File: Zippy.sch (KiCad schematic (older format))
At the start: 0 parts

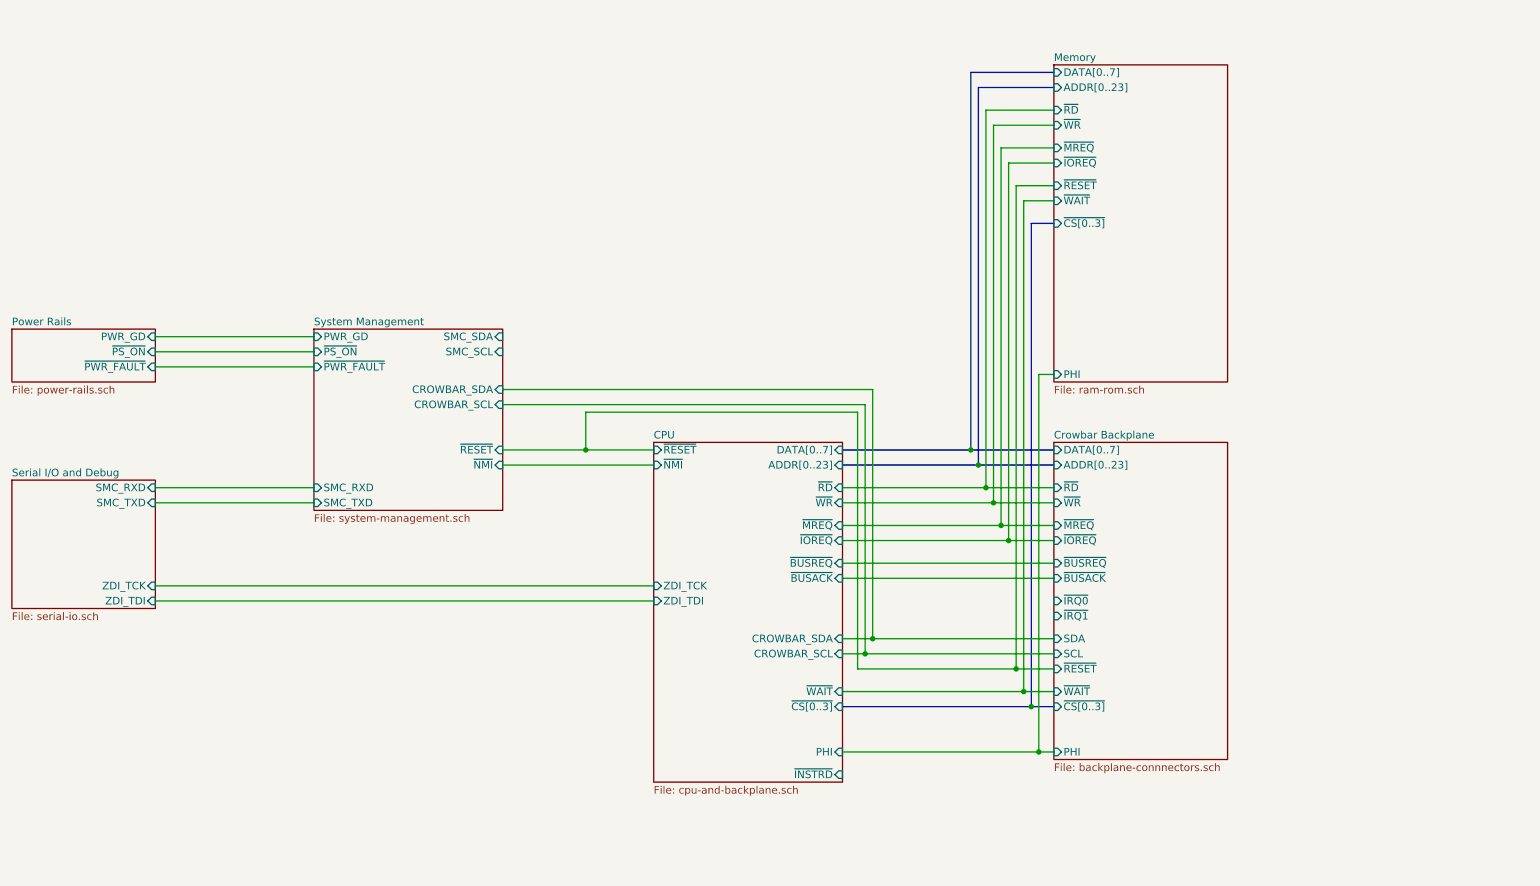
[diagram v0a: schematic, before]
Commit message: crowbar: Reworking the pinout again
  - Completely reworked the pinout of the crowbar bus to match the
    spec.
  - Added lines for eZ80 -> SMC I2C
  - Added lines for SMC -> Crowbar I2C
  - Migrated Crowbar power pinouts to their own sub-sheet
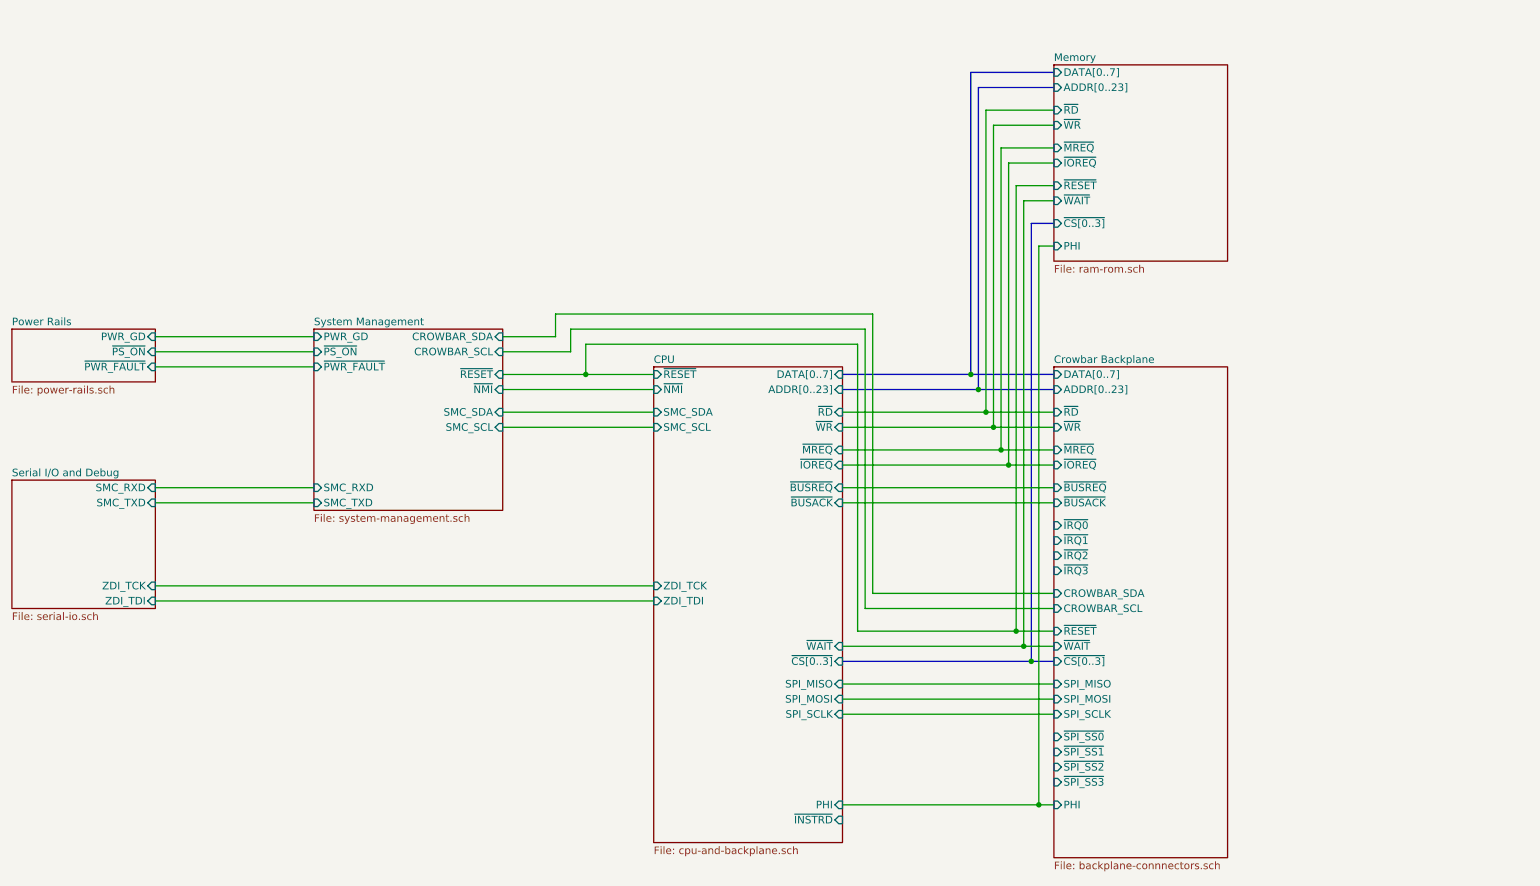
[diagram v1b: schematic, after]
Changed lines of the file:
@@
 $Descr A4 11693 8268
 encoding utf-8
-Sheet 1 7
+Sheet 1 8
 Title ""
 Date ""
@@
 $EndDescr
 $Sheet
-S 5650 3600 1250 2250
+S 5650 3100 1250 3150
 U 5D7F3F15
 F0 "CPU" 50
 F1 "cpu-and-backplane.sch" 50
-F2 "~RESET" I L 5650 3650 50
-F3 "PHI" I R 6900 5650 50
-F4 "ADDR[0..23]" I R 6900 3750 50
-F5 "DATA[0..7]" I R 6900 3650 50
-F6 "~CS[0..3]" I R 6900 5350 50
+F2 "~RESET" I L 5650 3150 50
+F3 "PHI" I R 6900 6000 50
+F4 "ADDR[0..23]" I R 6900 3250 50
+F5 "DATA[0..7]" I R 6900 3150 50
+F6 "~CS[0..3]" I R 6900 5050 50
 F7 "ZDI_TCK" I L 5650 4550 50
 F8 "ZDI_TDI" I L 5650 4650 50
-F9 "~NMI" I L 5650 3750 50
-F10 "CROWBAR_SCL" I R 6900 5000 50
-F11 "CROWBAR_SDA" I R 6900 4900 50
-F12 "~IOREQ" I R 6900 4250 50
-F13 "~MREQ" I R 6900 4150 50
-F14 "~RD" I R 6900 3900 50
-F15 "~WR" I R 6900 4000 50
-F16 "~INSTRD" I R 6900 5800 50
-F17 "~WAIT" I R 6900 5250 50
-F18 "~BUSREQ" I R 6900 4400 50
-F19 "~BUSACK" I R 6900 4500 50
+F9 "~NMI" I L 5650 3250 50
+F10 "~IOREQ" I R 6900 3750 50
+F11 "~MREQ" I R 6900 3650 50
+F12 "~RD" I R 6900 3400 50
+F13 "~WR" I R 6900 3500 50
+F14 "~INSTRD" I R 6900 6100 50
+F15 "~WAIT" I R 6900 4950 50
+F16 "~BUSREQ" I R 6900 3900 50
+F17 "~BUSACK" I R 6900 4000 50
+F18 "SMC_SCL" I L 5650 3500 50
+F19 "SMC_SDA" I L 5650 3400 50
+F20 "SPI_SCLK" I R 6900 5400 50
+F21 "SPI_MISO" I R 6900 5200 50
+F22 "SPI_MOSI" I R 6900 5300 50
 $EndSheet
 $Sheet
@@
 	2350 4650 5650 4650
 Wire Wire Line
-	4650 3650 5200 3650
-Wire Wire Line
-	4650 3750 5650 3750
-$Sheet
-S 8300 3600 1150 2100
+	4650 3150 5200 3150
+Wire Wire Line
+	4650 3250 5650 3250
+$Sheet
+S 8300 3100 1150 3250
 U 5D9D31F3
 F0 "Crowbar Backplane" 50
 F1 "backplane-connnectors.sch" 50
-F2 "DATA[0..7]" I L 8300 3650 50
-F3 "ADDR[0..23]" I L 8300 3750 50
-F4 "~RD" I L 8300 3900 50
-F5 "~WR" I L 8300 4000 50
-F6 "~MREQ" I L 8300 4150 50
-F7 "~IOREQ" I L 8300 4250 50
-F8 "~BUSREQ" I L 8300 4400 50
-F9 "~BUSACK" I L 8300 4500 50
-F10 "~IRQ0" I L 8300 4650 50
-F11 "~IRQ1" I L 8300 4750 50
-F12 "SDA" I L 8300 4900 50
-F13 "SCL" I L 8300 5000 50
-F14 "~WAIT" I L 8300 5250 50
-F15 "PHI" I L 8300 5650 50
-F16 "~RESET" I L 8300 5100 50
-F17 "~CS[0..3]" I L 8300 5350 50
-$EndSheet
-Wire Bus Line
-	6900 3650 7750 3650
-Wire Bus Line
-	6900 3750 7800 3750
-Wire Wire Line
-	6900 3900 7850 3900
-Wire Wire Line
-	6900 4000 7900 4000
-Wire Wire Line
-	6900 4150 7950 4150
-Wire Wire Line
-	6900 4250 8000 4250
-Wire Wire Line
-	6900 4400 8300 4400
-Wire Wire Line
-	6900 4500 8300 4500
-Wire Wire Line
-	6900 4900 7100 4900
-Wire Wire Line
-	6900 5000 7050 5000
-Wire Bus Line
-	6900 5350 8150 5350
-Wire Wire Line
-	6900 5250 8100 5250
-Wire Wire Line
-	7100 3250 7100 4900
-Wire Wire Line
-	4650 3250 7100 3250
-Connection ~ 7100 4900
-Wire Wire Line
-	7100 4900 8300 4900
-Wire Wire Line
-	7050 3350 7050 5000
-Wire Wire Line
-	4650 3350 7050 3350
-Connection ~ 7050 5000
-Wire Wire Line
-	7050 5000 8300 5000
-Wire Wire Line
-	5200 3650 5200 3400
-Wire Wire Line
-	5200 3400 7000 3400
-Wire Wire Line
-	7000 3400 7000 5100
-Wire Wire Line
-	7000 5100 8050 5100
-Connection ~ 5200 3650
-Wire Wire Line
-	5200 3650 5650 3650
-Wire Wire Line
-	6900 5650 8200 5650
+F2 "DATA[0..7]" I L 8300 3150 50
+F3 "ADDR[0..23]" I L 8300 3250 50
+F4 "~RD" I L 8300 3400 50
+F5 "~WR" I L 8300 3500 50
+F6 "~MREQ" I L 8300 3650 50
+F7 "~IOREQ" I L 8300 3750 50
+F8 "~BUSREQ" I L 8300 3900 50
+F9 "~BUSACK" I L 8300 4000 50
+F10 "~IRQ0" I L 8300 4150 50
+F11 "~IRQ1" I L 8300 4250 50
+F12 "~WAIT" I L 8300 4950 50
+F13 "PHI" I L 8300 6000 50
+F14 "~RESET" I L 8300 4850 50
+F15 "~CS[0..3]" I L 8300 5050 50
+F16 "~IRQ2" I L 8300 4350 50
+F17 "~IRQ3" I L 8300 4450 50
+F18 "~SPI_SS0" I L 8300 5550 50
+F19 "~SPI_SS1" I L 8300 5650 50
+F20 "~SPI_SS2" I L 8300 5750 50
+F21 "~SPI_SS3" I L 8300 5850 50
+F22 "SPI_MISO" I L 8300 5200 50
+F23 "SPI_MOSI" I L 8300 5300 50
+F24 "SPI_SCLK" I L 8300 5400 50
+F25 "CROWBAR_SDA" I L 8300 4600 50
+F26 "CROWBAR_SCL" I L 8300 4700 50
+$EndSheet
+Wire Bus Line
+	6900 3150 7750 3150
+Wire Bus Line
+	6900 3250 7800 3250
+Wire Wire Line
+	6900 3400 7850 3400
+Wire Wire Line
+	6900 3500 7900 3500
+Wire Wire Line
+	6900 3650 7950 3650
+Wire Wire Line
+	6900 3750 8000 3750
+Wire Wire Line
+	6900 3900 8300 3900
+Wire Wire Line
+	6900 4000 8300 4000
+Wire Bus Line
+	6900 5050 8150 5050
+Wire Wire Line
+	6900 4950 8100 4950
+Wire Wire Line
+	7100 2750 7100 4600
+Wire Wire Line
+	5000 2750 7100 2750
+Wire Wire Line
+	7100 4600 8300 4600
+Wire Wire Line
+	7050 2850 7050 4700
+Wire Wire Line
+	5100 2850 7050 2850
+Wire Wire Line
+	7050 4700 8300 4700
+Wire Wire Line
+	5200 3150 5200 2950
+Wire Wire Line
+	5200 2950 7000 2950
+Wire Wire Line
+	7000 2950 7000 4850
+Wire Wire Line
+	7000 4850 8050 4850
+Connection ~ 5200 3150
+Wire Wire Line
+	5200 3150 5650 3150
 $Sheet
 S 3400 2850 1250 1200
@@
 F0 "System Management" 50
 F1 "system-management.sch" 50
-F2 "~RESET" I R 4650 3650 50
+F2 "~RESET" I R 4650 3150 50
 F3 "SMC_RXD" I L 3400 3900 50
 F4 "SMC_TXD" I L 3400 4000 50
-F5 "CROWBAR_SDA" I R 4650 3250 50
-F6 "CROWBAR_SCL" I R 4650 3350 50
-F7 "~NMI" I R 4650 3750 50
-F8 "SMC_SDA" I R 4650 2900 50
-F9 "SMC_SCL" I R 4650 3000 50
+F5 "CROWBAR_SDA" I R 4650 2900 50
+F6 "CROWBAR_SCL" I R 4650 3000 50
+F7 "~NMI" I R 4650 3250 50
+F8 "SMC_SDA" I R 4650 3400 50
+F9 "SMC_SCL" I R 4650 3500 50
 F10 "~PS_ON" I L 3400 3000 50
 F11 "~PWR_FAULT" I L 3400 3100 50
 F12 "PWR_GD" I L 3400 2900 50
 $EndSheet
-$Sheet
-S 8300 1100 1150 2100
+Wire Bus Line
+	7750 3150 7750 1150
+Wire Bus Line
+	7750 1150 8300 1150
+Connection ~ 7750 3150
+Wire Bus Line
+	7750 3150 8300 3150
+Wire Bus Line
+	7800 3250 7800 1250
+Wire Bus Line
+	7800 1250 8300 1250
+Connection ~ 7800 3250
+Wire Bus Line
+	7800 3250 8300 3250
+Wire Wire Line
+	7850 3400 7850 1400
+Wire Wire Line
+	7850 1400 8300 1400
+Connection ~ 7850 3400
+Wire Wire Line
+	7850 3400 8300 3400
+Wire Wire Line
+	7900 3500 7900 1500
+Wire Wire Line
+	7900 1500 8300 1500
+Connection ~ 7900 3500
+Wire Wire Line
+	7900 3500 8300 3500
+Wire Wire Line
+	7950 3650 7950 1650
+Wire Wire Line
+	7950 1650 8300 1650
+Connection ~ 7950 3650
+Wire Wire Line
+	7950 3650 8300 3650
+Wire Wire Line
+	8000 3750 8000 1750
+Wire Wire Line
+	8000 1750 8300 1750
+Connection ~ 8000 3750
+Wire Wire Line
+	8000 3750 8300 3750
+Wire Wire Line
+	8050 4850 8050 1900
+Wire Wire Line
+	8050 1900 8300 1900
+Connection ~ 8050 4850
+Wire Wire Line
+	8050 4850 8300 4850
+Wire Wire Line
+	8100 4950 8100 2000
+Wire Wire Line
+	8100 2000 8300 2000
+Connection ~ 8100 4950
+Wire Wire Line
+	8100 4950 8300 4950
+Wire Bus Line
+	8150 5050 8150 2150
+Wire Bus Line
+	8150 2150 8300 2150
+Connection ~ 8150 5050
+Wire Bus Line
+	8150 5050 8300 5050
+Wire Wire Line
+	8200 6000 8200 2300
+Wire Wire Line
+	8200 2300 8300 2300
+Wire Wire Line
+	2350 3100 3400 3100
+Wire Wire Line
+	4650 3400 5650 3400
+Wire Wire Line
+	4650 3500 5650 3500
+Wire Wire Line
+	6900 6000 8200 6000
+Connection ~ 8200 6000
+Wire Wire Line
+	8200 6000 8300 6000
+$Sheet
+S 8300 1100 1150 1300
 U 5DCC6C4D
 F0 "Memory" 50
@@
 F9 "~WAIT" I L 8300 2000 50
 F10 "~CS[0..3]" I L 8300 2150 50
-F11 "PHI" I L 8300 3150 50
-$EndSheet
-Wire Bus Line
-	7750 3650 7750 1150
-Wire Bus Line
-	7750 1150 8300 1150
-Connection ~ 7750 3650
-Wire Bus Line
-	7750 3650 8300 3650
-Wire Bus Line
-	7800 3750 7800 1250
-Wire Bus Line
-	7800 1250 8300 1250
-Connection ~ 7800 3750
-Wire Bus Line
-	7800 3750 8300 3750
-Wire Wire Line
-	7850 3900 7850 1400
-Wire Wire Line
-	7850 1400 8300 1400
-Connection ~ 7850 3900
-Wire Wire Line
-	7850 3900 8300 3900
-Wire Wire Line
-	7900 4000 7900 1500
-Wire Wire Line
-	7900 1500 8300 1500
-Connection ~ 7900 4000
-Wire Wire Line
-	7900 4000 8300 4000
-Wire Wire Line
-	7950 4150 7950 1650
-Wire Wire Line
-	7950 1650 8300 1650
-Connection ~ 7950 4150
-Wire Wire Line
-	7950 4150 8300 4150
-Wire Wire Line
-	8000 4250 8000 1750
-Wire Wire Line
-	8000 1750 8300 1750
-Connection ~ 8000 4250
-Wire Wire Line
-	8000 4250 8300 4250
-Wire Wire Line
-	8050 5100 8050 1900
-Wire Wire Line
-	8050 1900 8300 1900
-Connection ~ 8050 5100
-Wire Wire Line
-	8050 5100 8300 5100
-Wire Wire Line
-	8100 5250 8100 2000
-Wire Wire Line
-	8100 2000 8300 2000
-Connection ~ 8100 5250
-Wire Wire Line
-	8100 5250 8300 5250
-Wire Bus Line
-	8150 5350 8150 2150
-Wire Bus Line
-	8150 2150 8300 2150
-Connection ~ 8150 5350
-Wire Bus Line
-	8150 5350 8300 5350
-Wire Wire Line
-	8200 5650 8200 3150
-Wire Wire Line
-	8200 3150 8300 3150
-Connection ~ 8200 5650
-Wire Wire Line
-	8200 5650 8300 5650
-Wire Wire Line
-	2350 3100 3400 3100
+F11 "PHI" I L 8300 2300 50
+$EndSheet
+Wire Wire Line
+	5100 2850 5100 3000
+Wire Wire Line
+	5100 3000 4650 3000
+Wire Wire Line
+	5000 2750 5000 2900
+Wire Wire Line
+	5000 2900 4650 2900
+Wire Wire Line
+	6900 5200 8300 5200
+Wire Wire Line
+	8300 5300 6900 5300
+Wire Wire Line
+	6900 5400 8300 5400
 $EndSCHEMATC

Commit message: toplevel: Add in SPI_SSx, IRQx, and INSTRD
  - Create the SPI_SSx and IRQx pins in the CPU schematic
  - Create the INSTRD pin in the memory schematic
  - Wire things up on the toplevel
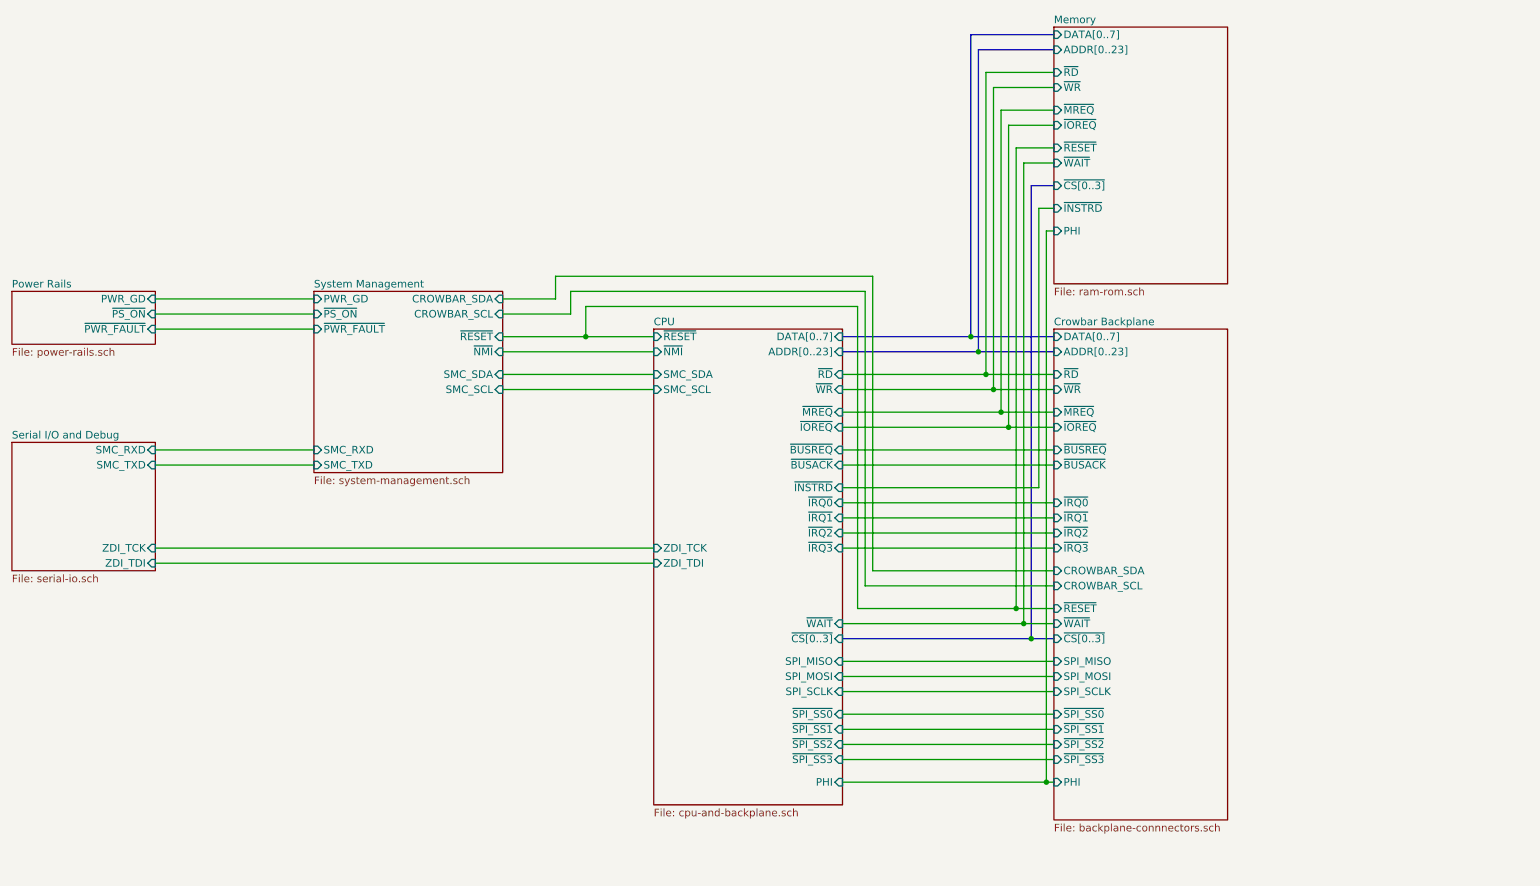
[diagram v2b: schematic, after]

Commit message: Major rework of the system RAM integration   - Wired up the jellybean logic for the RAM chip selects.   - Reorganized various bits here and there.   - Added preliminary symbols for the jellybean logic.
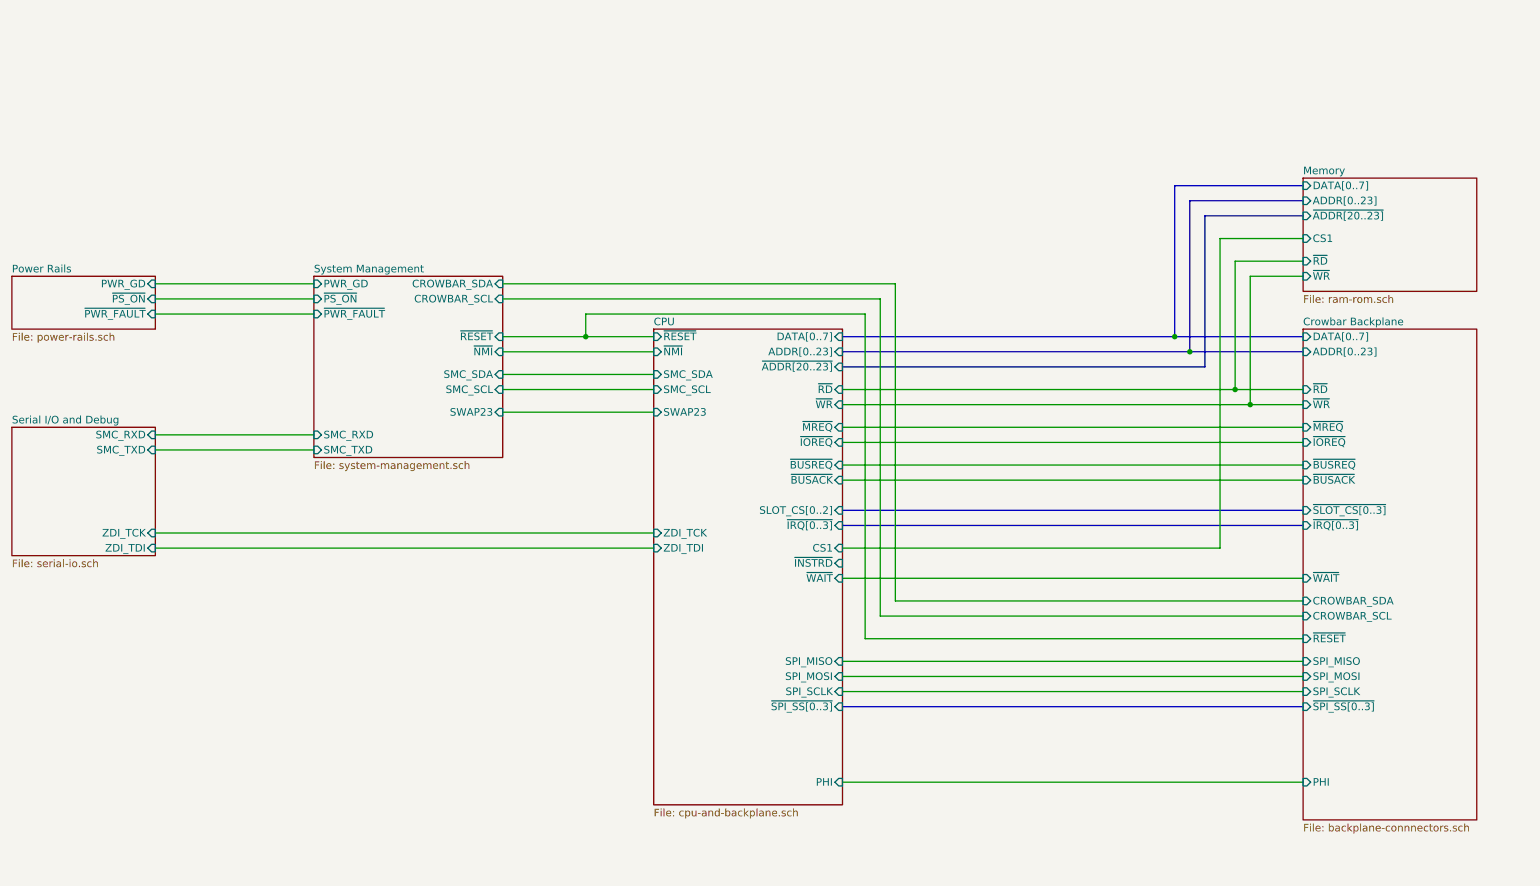
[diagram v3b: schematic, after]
